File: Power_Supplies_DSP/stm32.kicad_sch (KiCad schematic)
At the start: 30 parts, among them U2 STM32H755ZIT6, X3 NX3215SA-32.768K, X4 NX2016SA-32MHZ

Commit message: STM32 schematic no HS USB
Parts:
- added J1, J3, J4: Conn_01x10_Socket, symbol Connector:Conn_01x10_Socket
- added J2: SBH11-PBPC-D10-ST-BK, 2.54Pitch 20pin JTAG, symbol SDLibrary:SBH11-PBPC-D10-ST-BK
- added R13, R14, R15: 10k, Resistor_SMD:R_0805_2012Metric, symbol Device:R
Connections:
- net 3.3V: now also J2.1, J2.2, J4.1 (Pin_1)
- net 3.3V_2: now also J4.9 (Pin_9)
- net AGND: now also J4.10 (Pin_10)
- net GND: now also J2.10, J2.12, J2.14, J2.16, J2.18, J2.20, J2.4, J2.6, J2.8, J4.2 (Pin_2), R13.2, R14.2, R15.2
- net SWCLK: now also J2.9
- net SWDIO: now also J2.7
- net JTDI: now reaches U2.108 (PA15)
- net JTDI: now also J2.5
- net SPI3_SCK: now reaches U2.109 (PC10)
- net SPI3_SCK: now also J3.3 (Pin_3)
- net SPI3_MISO: now reaches U2.110 (PC11)
- net SPI3_MISO: now also J3.2 (Pin_2)
- net SPI3_MOSI: now reaches U2.111 (PC12)
- net SPI3_MOSI: now also J3.1 (Pin_1)
- net JTDO_SWO: now reaches U2.130 (PB3)
- net JTDO_SWO: now also J2.13
- net JTRST: now reaches U2.131 (PB4)
- net JTRST: now also J2.3
- net SAI2_FS_B: now reaches U2.28 (PC0)
- net SAI2_FS_B: now also J1.7 (Pin_7)
- net SAI2_SD_B: now reaches U2.37 (PA0)
- net SAI2_SD_B: now also J1.8 (Pin_8)
- net SAI2_MCLK_B: now reaches U2.38 (PA1)
- net SAI2_MCLK_B: now also J1.9 (Pin_9)
- net SAI2_SCK_B: now reaches U2.39 (PA2)
- net SAI2_SCK_B: now also J1.10 (Pin_10)
- net I2C3_SCL: now reaches U2.97 (PA8)
- net I2C3_SCL: now also J3.10 (Pin_10)
- net I2C3_SDA: now reaches U2.98 (PA9)
- net I2C3_SDA: now also J3.9 (Pin_9)
- net SAI1_MCLK_A: now reaches U2.1 (PE2)
- net SAI1_MCLK_A: now also J1.1 (Pin_1)
- net SAI1_SD_B: now reaches U2.2 (PE3)
- net SAI1_SD_B: now also J1.2 (Pin_2)
- net SAI1_FS_A: now reaches U2.3 (PE4)
- net SAI1_FS_A: now also J1.3 (Pin_3)
- net SAI1_SCK_A: now reaches U2.4 (PE5)
- net SAI1_SCK_A: now also J1.4 (Pin_4)
- net SAI1_SD_A: now reaches U2.5 (PE6)
- net SAI1_SD_A: now also J1.5 (Pin_5)
- net I2C4_SCL: now reaches U2.53 (PF14)
- net I2C4_SDA: now reaches U2.54 (PF15)
- new net: J2.11, R13.1
- new net: J2.17, R14.1
- new net: J2.19, R15.1
- no-connect marks 1 -> 2
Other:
- note added: "Debug Header"
- note added: "I2C Bus for ADC/DAC config"
- note added: "I2C3 (from MCU) pins for Raspberry Pi"
- note added: "Loading caps = 2*(crystal_load_cap - stray_cap)"
- note added: "Main Board Headers"
- note added: "Pins for ADCs ADC_A in master mode with MCLK ADC_B in synchronous slave"
- note added: "Pins for DAC (Plus SAI2_FS_B)"
- note added: "Raspberry Pi Headers"
- note added: "SPI3 (from MCU) pins for Raspberry Pi"
- moved on the sheet: C10, C11, C12, C13, C14, C15, C16, C17, C18, C19, C20, C21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

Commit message: mcu PCB
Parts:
- removed J1, J3, J4: Conn_01x10_Socket, symbol Connector:Conn_01x10_Socket
- added C27, C28: 0.01uF, Capacitor_SMD:C_0603_1608Metric_Pad1.08x0.95mm_HandSolder, symbol Device:C
- added C29, C30: 100nF, Capacitor_SMD:C_0603_1608Metric_Pad1.08x0.95mm_HandSolder, symbol Device:C
- added J1, J4: PINHD_1x10_Male, Connector_PinHeader_2.54mm:PinHeader_1x10_P2.54mm_Vertical, symbol PCM_SL_Pin_Headers:PINHD_1x10_Male
- added J5: PINHD_1x2_Female, Connector_PinSocket_2.54mm:PinSocket_1x02_P2.54mm_Vertical, symbol PCM_SL_Pin_Headers:PINHD_1x2_Female
- added J6: PINHD_1x10_Female, Connector_PinSocket_2.54mm:PinSocket_1x10_P2.54mm_Vertical, symbol PCM_SL_Pin_Headers:PINHD_1x10_Female
- added R10, R11, R8, R9: 10k, Resistor_SMD:R_0805_2012Metric, symbol Device:R
- added U3: PEC11R-4030F-N0024, SamacSys_Parts:PEC11R4030FN0024, symbol SamacSys_Parts:PEC11R-4030F-N0024
- C10, C11, C12, C13, C14, C15, C16, C17, C18, C19, C20, C21, C22, C23, C24, C25, C26, C3, C4, C5, C6, C7, C8, C9: footprint Capacitor_SMD:C_0402_1005Metric -> Capacitor_SMD:C_0603_1608Metric_Pad1.08x0.95mm_HandSolder
- J2: footprint 2.54Pitch 20pin JTAG -> SamacSys_Parts:FTSH-110-XX-YYY-DV-K
- U2: footprint LQFP-144 -> SamacSys_Parts:QFP50P2200X2200X160-144N
- X4: footprint (none) -> SamacSys_Parts:FA-238_EPS
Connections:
- net 3.3V: now also C29.1, C30.1, J1.2
- net 3.3V_2: now also J1.9
- net AGND: now also J1.10
- net GND: now also C27.1, C28.2, C29.2, C30.2, J1.1, J6.6
- net I2C3_SCL: now also J6.10
- net I2C3_SDA: now also J6.9
- net I2C4_SCL: now also J1.7
- net I2C4_SDA: now also J1.6
- net SAI1_FS_A: now also J4.3
- net SAI1_MCLK_A: now also J4.1
- net SAI1_SCK_A: now also J4.4
- net SAI1_SD_B: now also J4.2
- net SAI2_FS_B: now also J4.7
- net SAI2_MCLK_B: now also J4.9
- net SAI2_SCK_B: now also J4.10
- net SAI2_SD_B: now also J4.8
- net SPI3_MISO: now also J6.2
- net SPI3_MOSI: now also J6.1
- net SPI3_SCK: now also J6.3
- net SAI1_SD_A: no longer names the net of U2.5 (PE6)
- new net: R10.2, R11.1
- new net: R8.2, R9.1
- new net 5V: J1.3, R10.1, R8.1
- new net Rotary+: C27.2, J5.1, J6.5, R9.2
- new net Rotary-: C28.1, J5.2, J6.7, R11.2
- no-connect marks 2 -> 4
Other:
- note added: "PEC11R-4030F-N0024"
- note added: "Rotary Encoder"
- note added: "SAI1_FS_A = LRCK SAI_SCK_A = BCLK Both Douts of ADCs merge into one pin, SAI1_SD_B"
- note added: "SAI2_SCK_B = BCLK SAI2_FS-B = LRCK SAI2_SD_B = DIN"

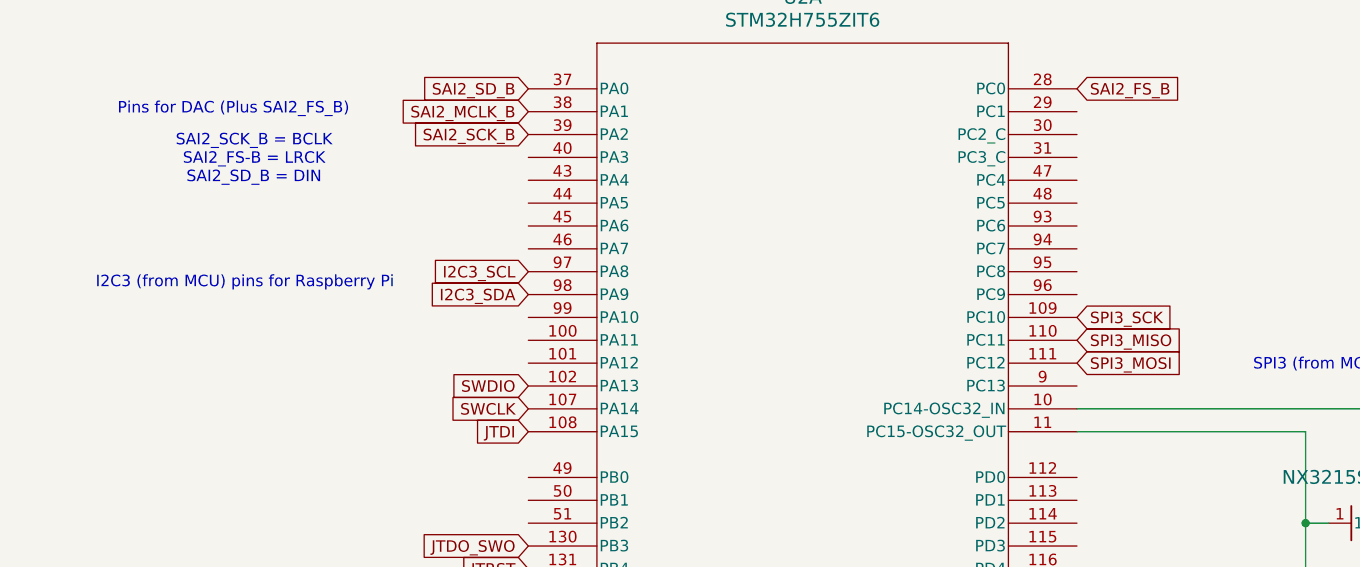
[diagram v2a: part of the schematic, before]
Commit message: added USB + fixed one routing on original DSP board
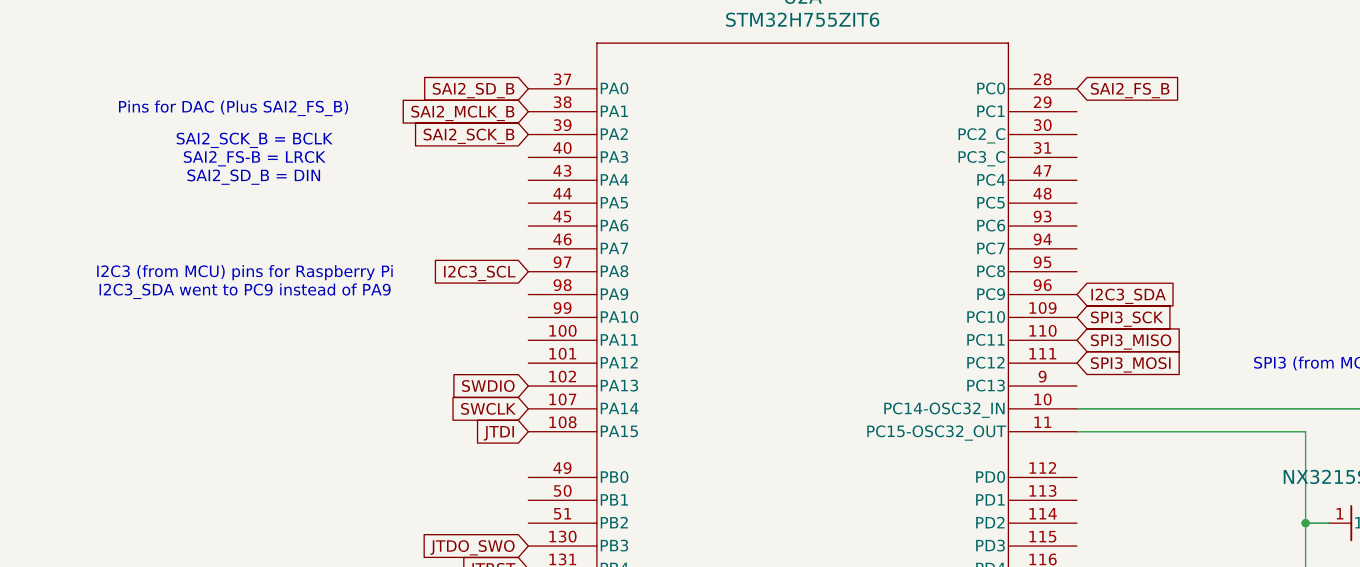
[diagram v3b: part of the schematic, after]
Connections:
- net I2C3_SDA: now also U2.96 (PC9); no longer U2.98 (PA9)
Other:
- note added: "I2C3 (from MCU) pins for Raspberry Pi I2C3_SDA went to PC9 instead of PA9"
- note removed: "I2C3 (from MCU) pins for Raspberry Pi"
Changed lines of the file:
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@@
 		)
 	)
-	(text "I2C3 (from MCU) pins for Raspberry Pi"
+	(text "I2C3 (from MCU) pins for Raspberry Pi\nI2C3_SDA went to PC9 instead of PA9"
 		(exclude_from_sim no)
 		(at 66.294 257.81 0)
@@
 		)
 	)
+	(global_label "I2C3_SDA"
+		(shape input)
+		(at 158.75 259.08 0)
+		(fields_autoplaced yes)
+		(effects
+			(font
+				(size 1.27 1.27)
+			)
+			(justify left)
+		)
+		(property "Intersheetrefs" "${INTERSHEET_REFS}"
+			(at 170.5647 259.08 0)
+			(effects
+				(font
+					(size 1.27 1.27)
+				)
+				(justify left)
+				(hide yes)
+			)
+		)
+	)
 	(global_label "I2C3_SCL"
 		(shape input)
@@
 				(hide yes)
 			)
-		)
-	)
-	(global_label "I2C3_SDA"
-		(shape input)
-		(at 97.79 259.08 180)
-		(fields_autoplaced yes)
-		(effects
-			(font
-				(size 1.27 1.27)
-			)
-			(justify right)
-		)
-		(property "Intersheetrefs" "${INTERSHEET_REFS}"
-			(at 85.9753 259.08 0)
-			(effects
-				(font
-					(size 1.27 1.27)
-				)
-				(justify right)
-				(hide yes)
-			)

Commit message: fixed pcb conexions
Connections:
- net SAI2_MCLK_B: no longer U2.38 (PA1)
- net Rotary+ renamed CHANNEL_1
- net Rotary- renamed CHANNEL_2
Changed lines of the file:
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@@
 	(wire
 		(pts
-			(xy 488.95 80.01) (xy 513.08 80.01)
-		)
-		(stroke
-			(width 0)
-			(type default)
-		)
-	)
-	(wire
-		(pts
 			(xy 464.82 251.46) (xy 468.63 251.46)
 		)
@@
 		)
 	)
-	(global_label "Rotary+"
+	(global_label "CHANNEL_1"
 		(shape input)
 		(at 349.25 72.39 180)
@@
 		)
 		(property "Intersheetrefs" "${INTERSHEET_REFS}"
-			(at 338.6449 72.39 0)
+			(at 335.5605 72.39 0)
 			(effects
 				(font
@@
 		)
 	)
-	(global_label "Rotary_Ground"
-		(shape input)
-		(at 513.08 80.01 0)
-		(fields_autoplaced yes)
-		(effects
-			(font
-				(size 1.27 1.27)
-			)
-			(justify left)
-		)
-		(property "Intersheetrefs" "${INTERSHEET_REFS}"
-			(at 529.7325 80.01 0)
-			(effects
-				(font
-					(size 1.27 1.27)
-				)
-				(justify left)
-				(hide yes)
-			)
-		)
-	)
-	(global_label "SAI2_MCLK_B"
-		(shape input)
-		(at 97.79 238.76 180)
-		(fields_autoplaced yes)
-		(effects
-			(font
-				(size 1.27 1.27)
-			)
-			(justify right)
-		)
-		(property "Intersheetrefs" "${INTERSHEET_REFS}"
-			(at 82.4677 238.76 0)
-			(effects
-				(font
-					(size 1.27 1.27)
-				)
-				(justify right)
-				(hide yes)
-			)
-		)
-	)
 	(global_label "3.3V"
 		(shape input)
@@
 		)
 	)
-	(global_label "Rotary-"
+	(global_label "CHANNEL_2"
 		(shape input)
 		(at 513.08 82.55 0)
@@
 		)
 		(property "Intersheetrefs" "${INTERSHEET_REFS}"
-			(at 523.6851 82.55 0)
+			(at 526.7695 82.55 0)
 			(effects
 				(font
@@
 		)
 	)
-	(global_label "Rotary-"
+	(global_label "CHANNEL_2"
 		(shape input)
 		(at 349.25 77.47 180)
@@
 		)
 		(property "Intersheetrefs" "${INTERSHEET_REFS}"
-			(at 338.6449 77.47 0)
+			(at 335.5605 77.47 0)
 			(effects
 				(font
@@
 		)
 	)
-	(global_label "Rotary+"
+	(global_label "CHANNEL_1"
 		(shape input)
 		(at 513.08 77.47 0)
@@
 		)
 		(property "Intersheetrefs" "${INTERSHEET_REFS}"
-			(at 523.6851 77.47 0)
+			(at 526.7695 77.47 0)
 			(effects
 				(font
@@
 		)
 	)
-	(global_label "Rotary_Ground"
-		(shape input)
-		(at 349.25 74.93 180)
-		(fields_autoplaced yes)
-		(effects
-			(font
-				(size 1.27 1.27)
-			)
-			(justify right)
-		)
-		(property "Intersheetrefs" "${INTERSHEET_REFS}"
-			(at 332.5975 74.93 0)
-			(effects
-				(font
-					(size 1.27 1.27)
-				)
-				(justify right)
-				(hide yes)
-			)
-		)
-	)
 	(global_label "3.3V"
 		(shape input)
@@
 		)
 	)
+	(global_label "SAI2_MCLK_B"
+		(shape input)
+		(at 95.25 238.76 180)
+		(fields_autoplaced yes)
+		(effects
+			(font
+				(size 1.27 1.27)
+			)
+			(justify right)
+		)
+		(property "Intersheetrefs" "${INTERSHEET_REFS}"
+			(at 79.9277 238.76 0)
+			(effects
+				(font
+					(size 1.27 1.27)
+				)
+				(justify right)
+				(hide yes)
+			)
+		)
+	)
 	(global_label "SAI1_FS_A"
 		(shape input)
@@
 	(symbol
 		(lib_id "power:GND")
+		(at 349.25 74.93 270)
+		(unit 1)
+		(exclude_from_sim no)
+		(in_bom yes)
+		(on_board yes)
+		(dnp no)
+		(fields_autoplaced yes)
+		(property "Reference" "#PWR023"
+			(at 342.9 74.93 0)
+			(effects
+				(font
+					(size 1.27 1.27)
+				)
+				(hide yes)
+			)
+		)
+		(property "Value" "GND"
+			(at 345.44 74.9299 90)
+			(effects
+				(font
+					(size 1.27 1.27)
+				)
+				(justify right)
+			)
+		)
+		(property "Footprint" ""
+			(at 349.25 74.93 0)
+			(effects
+				(font
+					(size 1.27 1.27)
+				)
+				(hide yes)
+			)
+		)
+		(property "Datasheet" ""
+			(at 349.25 74.93 0)
+			(effects
+				(font
+					(size 1.27 1.27)
+				)
+				(hide yes)
+			)
+		)
+		(property "Description" "Power symbol creates a global label with name \"GND\" , ground"
+			(at 349.25 74.93 0)
+			(effects
+				(font
+					(size 1.27 1.27)
+				)
+				(hide yes)
+			)
+		)
+		(pin "1"
+		)
+		(instances
+			(project "Power_Supplies_DSP"
+				(path "/5266cf9e-da90-4c53-80fd-cf3dbed42632/3fb43f8a-8ac2-41bd-9c44-03d9d8c3e7fe"
+					(reference "#PWR023")
+					(unit 1)
+				)
+			)
+		)
+	)
+	(symbol
+		(lib_id "power:GND")
 		(at 386.08 269.24 0)
 		(unit 1)
@@
 					(unit 1)
 				)
-			)
-		)
-	)
-	(symbol
-		(lib_id "power:GND")
-		(at 488.95 80.01 0)
-		(unit 1)
-		(exclude_from_sim no)
-		(in_bom yes)
-		(on_board yes)
-		(dnp no)
-		(fields_autoplaced yes)
-		(property "Reference" "#PWR023"
-			(at 488.95 86.36 0)
-			(effects
-				(font
-					(size 1.27 1.27)
-				)
-				(hide yes)
-			)
-		)
-		(property "Value" "GND"
-			(at 488.95 85.09 0)
-			(effects
-				(font
-					(size 1.27 1.27)
-				)
-			)
-		)
-		(property "Footprint" ""
-			(at 488.95 80.01 0)
-			(effects
-				(font
-					(size 1.27 1.27)
-				)
-				(hide yes)
-			)
-		)
-		(property "Datasheet" ""
-			(at 488.95 80.01 0)
-			(effects
-				(font
-					(size 1.27 1.27)
-				)
-				(hide yes)
-			)
-		)
-		(property "Description" "Power symbol creates a global label with name \"GND\" , ground"
-			(at 488.95 80.01 0)
-			(effects
-				(font
-					(size 1.27 1.27)
-				)
-				(hide yes)
-			)
-		)
-		(pin "1"
-		)
-		(instances
-			(project "Power_Supplies_DSP"
-				(path "/5266cf9e-da90-4c53-80fd-cf3dbed42632/3fb43f8a-8ac2-41bd-9c44-03d9d8c3e7fe"
-					(reference "#PWR023")
-					(unit 1)
-				)

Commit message: added changes that weeks wanted 🐷
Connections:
- net GND: now also U2.34 (VSSA)
- net AGND: no longer names the net of J1.10
- net AGND: no longer U2.34 (VSSA)
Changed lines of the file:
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@@
 	)
 	(junction
+		(at 537.21 276.86)
+		(diameter 0)
+		(color 0 0 0 0)
+	)
+	(junction
 		(at 438.15 302.26)
 		(diameter 0)
@@
 	(wire
 		(pts
+			(xy 537.21 276.86) (xy 537.21 279.4)
+		)
+		(stroke
+			(width 0)
+			(type default)
+		)
+	)
+	(wire
+		(pts
 			(xy 199.39 271.78) (xy 199.39 284.48)
 		)
@@
 	(wire
 		(pts
+			(xy 537.21 276.86) (xy 547.37 276.86)
+		)
+		(stroke
+			(width 0)
+			(type default)
+		)
+	)
+	(wire
+		(pts
 			(xy 464.82 256.54) (xy 464.82 259.08)
 		)
@@
 	(wire
 		(pts
-			(xy 537.21 269.24) (xy 537.21 279.4)
+			(xy 537.21 269.24) (xy 537.21 276.86)
 		)
 		(stroke
@@
 	)
 	(symbol
-		(lib_id "power:GND")
-		(at 547.37 276.86 0)
-		(unit 1)
-		(exclude_from_sim no)
-		(in_bom yes)
-		(on_board yes)
-		(dnp no)
-		(fields_autoplaced yes)
-		(property "Reference" "#PWR06"
-			(at 547.37 283.21 0)
-			(effects
-				(font
-					(size 1.27 1.27)
-				)
-				(hide yes)
-			)
-		)
-		(property "Value" "AGND"
-			(at 547.37 281.94 0)
-			(effects
-				(font
-					(size 1.27 1.27)
-				)
-			)
-		)
-		(property "Footprint" ""
-			(at 547.37 276.86 0)
-			(effects
-				(font
-					(size 1.27 1.27)
-				)
-				(hide yes)
-			)
-		)
-		(property "Datasheet" ""
-			(at 547.37 276.86 0)
-			(effects
-				(font
-					(size 1.27 1.27)
-				)
-				(hide yes)
-			)
-		)
-		(property "Description" "Power symbol creates a global label with name \"GND\" , ground"
-			(at 547.37 276.86 0)
-			(effects
-				(font
-					(size 1.27 1.27)
-				)
-				(hide yes)
-			)
-		)
-		(pin "1"
-		)
-		(instances
-			(project "Power_Supplies_DSP"
-				(path "/5266cf9e-da90-4c53-80fd-cf3dbed42632/3fb43f8a-8ac2-41bd-9c44-03d9d8c3e7fe"
-					(reference "#PWR06")
-					(unit 1)
-				)
-			)
-		)
-	)
-	(symbol
 		(lib_id "PCM_SL_Pin_Headers:PINHD_1x2_Female")
 		(at 508 72.39 0)
@@
 					(unit 1)
 				)
-			)
-		)
-	)
-	(symbol
-		(lib_id "power:GND")
-		(at 275.59 83.82 0)
-		(unit 1)
-		(exclude_from_sim no)
-		(in_bom yes)
-		(on_board yes)
-		(dnp no)
-		(fields_autoplaced yes)
-		(property "Reference" "#PWR022"
-			(at 275.59 90.17 0)
-			(effects
-				(font
-					(size 1.27 1.27)
-				)
-				(hide yes)
-			)
-		)
-		(property "Value" "AGND"
-			(at 275.59 88.9 0)
-			(effects
-				(font
-					(size 1.27 1.27)
-				)
-			)
-		)
-		(property "Footprint" ""
-			(at 275.59 83.82 0)
-			(effects
-				(font
-					(size 1.27 1.27)
-				)
-				(hide yes)
-			)
-		)
-		(property "Datasheet" ""
-			(at 275.59 83.82 0)
-			(effects
-				(font
-					(size 1.27 1.27)
-				)
-				(hide yes)
-			)
-		)
-		(property "Description" "Power symbol creates a global label with name \"GND\" , ground"
-			(at 275.59 83.82 0)
-			(effects
-				(font
-					(size 1.27 1.27)
-				)
-				(hide yes)
-			)
-		)
-		(pin "1"
-		)
-		(instances
-			(project "Power_Supplies_DSP"
-				(path "/5266cf9e-da90-4c53-80fd-cf3dbed42632/3fb43f8a-8ac2-41bd-9c44-03d9d8c3e7fe"
-					(reference "#PWR022")
-					(unit 1)
-				)
